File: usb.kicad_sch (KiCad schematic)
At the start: 0 parts

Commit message: merged in USB
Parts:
- added IC1: USB Hub, QFP80P900X900X160-32N, symbol group127:USB Hub
- added J1, J2: 2-Port USB, CONN_AU-Y1008-2_ASM, symbol group127:2-Port USB

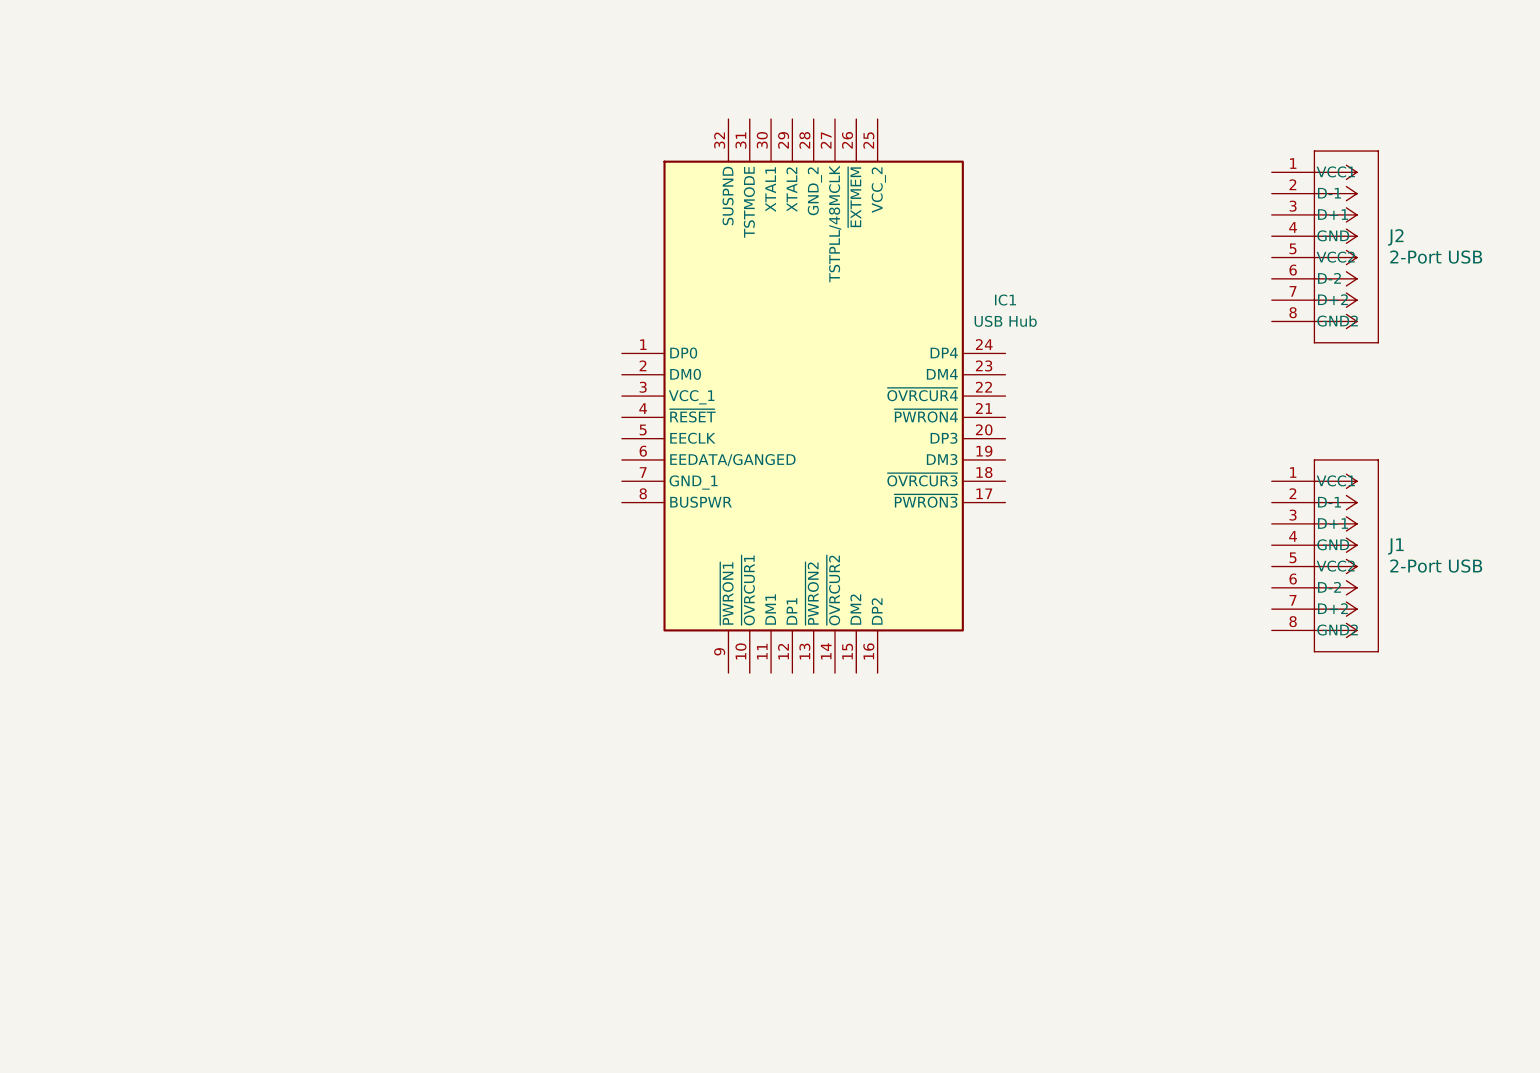
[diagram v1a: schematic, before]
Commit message: usb hub support completed
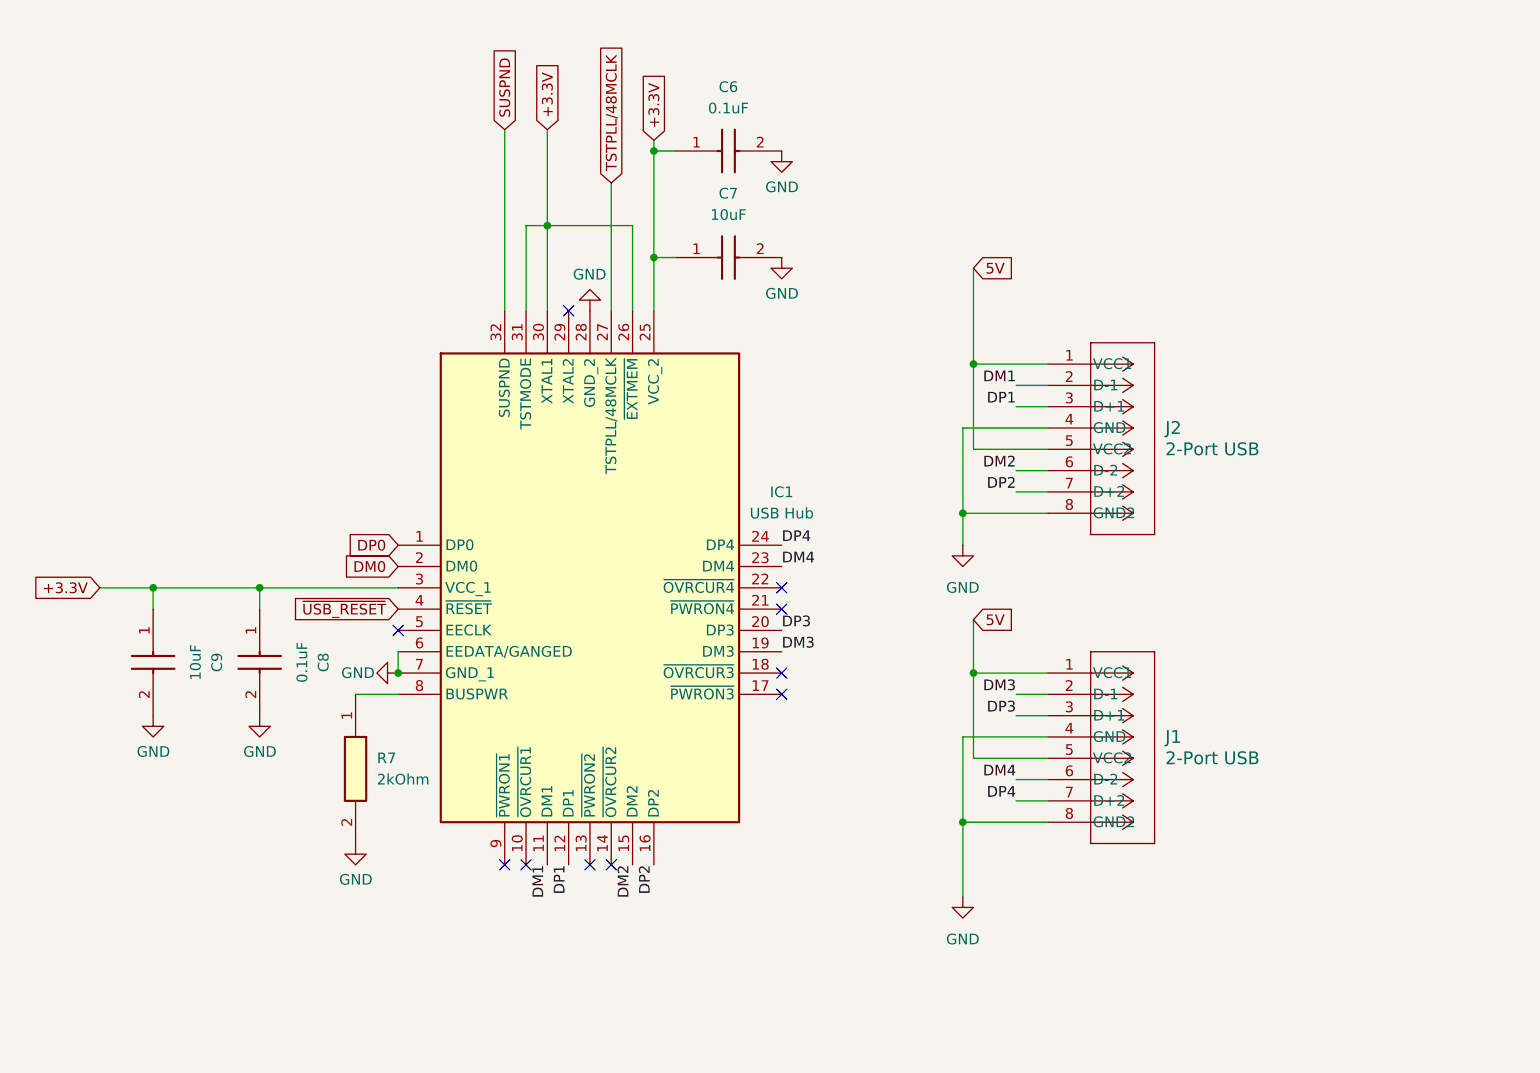
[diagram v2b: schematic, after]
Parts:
- added C6, C8: 0.1uF, CAPC2012X94N, symbol group127:0805Capacitor
- added C7, C9: 10uF, CAPC2012X94N, symbol group127:0805Capacitor
- added R7: 2kOhm, RESC2012X60N, symbol group127:Resistor
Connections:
- net 5V: now reaches J1.1 (VCC1)
- net 5V: now also J1.5 (VCC2), J2.1 (VCC1), J2.5 (VCC2)
- net DM3: now reaches J1.2 (D-1)
- net DM3: now also IC1.19 (DM3)
- net DP3: now reaches J1.3 (D+1)
- net DP3: now also IC1.20 (DP3)
- net GND: now reaches J1.4 (GND)
- net GND: now also IC1.28 (GND_2), IC1.6 (EEDATA/GANGED), IC1.7 (GND_1), J1.8 (GND2), J2.4 (GND), J2.8 (GND2), C6.2, C7.2, C8.2, C9.2, R7.2
- net DM4: now reaches J1.6 (D-2)
- net DM4: now also IC1.23 (DM4)
- net DP4: now reaches J1.7 (D+2)
- net DP4: now also IC1.24 (DP4)
- net DM1: now reaches J2.2 (D-1)
- net DM1: now also IC1.11 (DM1)
- net DP1: now reaches J2.3 (D+1)
- net DP1: now also IC1.12 (DP1)
- net DM2: now reaches J2.6 (D-2)
- net DM2: now also IC1.15 (DM2)
- net DP2: now reaches J2.7 (D+2)
- net DP2: now also IC1.16 (DP2)
- net DP0: now reaches IC1.1 (DP0)
- net DM0: now reaches IC1.2 (DM0)
- net +3.3V: now reaches IC1.25 (VCC_2)
- net +3.3V: now also IC1.26 (~{EXTMEM}), IC1.3 (VCC_1), IC1.30 (XTAL1), IC1.31 (TSTMODE), C6.1, C7.1, C8.1, C9.1
- net TSTPLL/48MCLK: now reaches IC1.27 (TSTPLL/48MCLK)
- net SUSPND: now reaches IC1.32 (SUSPND)
- net ~{USB_RESET}: now reaches IC1.4 (~{RESET})
- net at IC1.8 (BUSPWR): now also R7.1
- no-connect marks 0 -> 10
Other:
- moved on the sheet: IC1, J1, J2

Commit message: standardize 5V and 3V3 labels
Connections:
- net +3.3V renamed 3V3
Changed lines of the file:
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@@
 		)
 	)
-	(global_label "+3.3V"
+	(global_label "3V3"
+		(shape input)
+		(at 73.66 102.87 180)
+		(fields_autoplaced yes)
+		(effects
+			(font
+				(size 1.27 1.27)
+			)
+			(justify right)
+		)
+		(property "Intersheetrefs" "${INTERSHEET_REFS}"
+			(at 67.1672 102.87 0)
+			(effects
+				(font
+					(size 1.27 1.27)
+				)
+				(justify right)
+				(hide yes)
+			)
+		)
+	)
+	(global_label "3V3"
 		(shape input)
 		(at 139.7 49.53 90)
+		(fields_autoplaced yes)
 		(effects
 			(font
@@
 		)
 		(property "Intersheetrefs" "${INTERSHEET_REFS}"
-			(at 139.7 49.53 0)
+			(at 139.7 43.0372 90)
 			(effects
 				(font
 					(size 1.27 1.27)
 				)
+				(justify left)
 				(hide yes)
 			)
@@
 		)
 	)
-	(global_label "+3.3V"
-		(shape input)
-		(at 73.66 102.87 180)
-		(effects
-			(font
-				(size 1.27 1.27)
-			)
-			(justify right)
-		)
-		(property "Intersheetrefs" "${INTERSHEET_REFS}"
-			(at 73.66 102.87 0)
-			(effects
-				(font
-					(size 1.27 1.27)
-				)
-				(hide yes)
-			)
-		)
-	)
-	(global_label "+3.3V"
-		(shape input)
-		(at 127 48.26 90)
-		(effects
-			(font
-				(size 1.27 1.27)
-			)
-			(justify left)
-		)
-		(property "Intersheetrefs" "${INTERSHEET_REFS}"
-			(at 127 48.26 0)
-			(effects
-				(font
-					(size 1.27 1.27)
-				)
-				(hide yes)
-			)
-		)
-	)
 	(global_label "5V"
 		(shape input)
@@
 			(effects
 				(font
+					(size 1.27 1.27)
+				)
+				(justify left)
+				(hide yes)
+			)
+		)
+	)
+	(global_label "3V3"
+		(shape input)
+		(at 127 48.26 90)
+		(fields_autoplaced yes)
+		(effects
+			(font
+				(size 1.27 1.27)
+			)
+			(justify left)
+		)
+		(property "Intersheetrefs" "${INTERSHEET_REFS}"
+			(at 127 41.7672 90)
+			(effects
+				(font

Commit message: finished up schematic
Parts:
- C2: renamed from C9; footprint CAPC2012X94N -> Capacitor_SMD:C_0805_2012Metric
- C3: renamed from C8; footprint CAPC2012X94N -> Capacitor_SMD:C_0805_2012Metric
- C4: renamed from C6; footprint CAPC2012X94N -> Capacitor_SMD:C_0805_2012Metric
- C5: renamed from C7; footprint CAPC2012X94N -> Capacitor_SMD:C_0805_2012Metric
- IC2: renamed from IC1; footprint QFP80P900X900X160-32N -> (none)
- J2: footprint CONN_AU-Y1008-2_ASM -> (none)
- J3: renamed from J1; footprint CONN_AU-Y1008-2_ASM -> (none)
- R1: renamed from R7; footprint RESC2012X60N -> Resistor_SMD:R_0805_2012Metric
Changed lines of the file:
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@@
 		(dnp no)
 		(fields_autoplaced yes)
-		(property "Reference" "R7"
+		(property "Reference" "R1"
 			(at 106.68 123.1899 90)
 			(effects
@@
 			)
 		)
-		(property "Footprint" "RESC2012X60N"
+		(property "Footprint" "Resistor_SMD:R_0805_2012Metric"
 			(at 7.95 129.54 0)
 			(effects
@@
 			(project ""
 				(path "/5ce3566e-4e0f-420e-9b0d-3952cd3c63fd/5f7ff1a1-baeb-4db3-a7fc-b3c90c01be12"
-					(reference "R7")
+					(reference "R1")
 					(unit 1)
 				)
@@
 		(dnp no)
 		(fields_autoplaced yes)
-		(property "Reference" "C7"
+		(property "Reference" "C5"
 			(at 148.59 55.88 0)
 			(effects
@@
 			)
 		)
-		(property "Footprint" "CAPC2012X94N"
+		(property "Footprint" "Capacitor_SMD:C_0805_2012Metric"
 			(at 151.13 159.69 0)
 			(effects
@@
 			(project ""
 				(path "/5ce3566e-4e0f-420e-9b0d-3952cd3c63fd/5f7ff1a1-baeb-4db3-a7fc-b3c90c01be12"
-					(reference "C7")
+					(reference "C5")
 					(unit 1)
 				)
@@
 		(dnp no)
 		(fields_autoplaced yes)
-		(property "Reference" "J1"
+		(property "Reference" "J3"
 			(at 200.66 120.6499 0)
 			(effects
@@
 			)
 		)
-		(property "Footprint" "CONN_AU-Y1008-2_ASM"
+		(property "Footprint" ""
 			(at 179.324 135.382 0)
 			(effects
@@
 			(project ""
 				(path "/5ce3566e-4e0f-420e-9b0d-3952cd3c63fd/5f7ff1a1-baeb-4db3-a7fc-b3c90c01be12"
-					(reference "J1")
+					(reference "J3")
 					(unit 1)
 				)
@@
 		(on_board yes)
 		(dnp no)
-		(property "Reference" "#PWR015"
+		(property "Reference" "#PWR012"
 			(at 102.87 113.03 0)
 			(effects
@@
 			(project ""
 				(path "/5ce3566e-4e0f-420e-9b0d-3952cd3c63fd/5f7ff1a1-baeb-4db3-a7fc-b3c90c01be12"
-					(reference "#PWR015")
+					(reference "#PWR012")
 					(unit 1)
 				)
@@
 			)
 		)
-		(property "Footprint" "CONN_AU-Y1008-2_ASM"
+		(property "Footprint" ""
 			(at 179.324 98.552 0)
 			(effects
@@
 		(dnp no)
 		(fields_autoplaced yes)
-		(property "Reference" "C9"
+		(property "Reference" "C2"
 			(at 87.63 111.76 0)
 			(effects
@@
 			)
 		)
-		(property "Footprint" "CAPC2012X94N"
+		(property "Footprint" "Capacitor_SMD:C_0805_2012Metric"
 			(at -16.18 114.3 0)
 			(effects
@@
 			(project "harm_drone"
 				(path "/5ce3566e-4e0f-420e-9b0d-3952cd3c63fd/5f7ff1a1-baeb-4db3-a7fc-b3c90c01be12"
-					(reference "C9")
+					(reference "C2")
 					(unit 1)
 				)
@@
 		(on_board yes)
 		(dnp no)
-		(property "Reference" "#PWR019"
+		(property "Reference" "#PWR011"
 			(at 104.14 139.7 0)
 			(effects
@@
 			(project "harm_drone"
 				(path "/5ce3566e-4e0f-420e-9b0d-3952cd3c63fd/5f7ff1a1-baeb-4db3-a7fc-b3c90c01be12"
-					(reference "#PWR019")
+					(reference "#PWR011")
 					(unit 1)
 				)
@@
 		(dnp no)
 		(fields_autoplaced yes)
-		(property "Reference" "C8"
+		(property "Reference" "C3"
 			(at 100.33 111.76 0)
 			(effects
@@
 			)
 		)
-		(property "Footprint" "CAPC2012X94N"
+		(property "Footprint" "Capacitor_SMD:C_0805_2012Metric"
 			(at -3.48 114.3 0)
 			(effects
@@
 			(project "harm_drone"
 				(path "/5ce3566e-4e0f-420e-9b0d-3952cd3c63fd/5f7ff1a1-baeb-4db3-a7fc-b3c90c01be12"
-					(reference "C8")
+					(reference "C3")
 					(unit 1)
 				)
@@
 		(on_board yes)
 		(dnp no)
-		(property "Reference" "#PWR04"
+		(property "Reference" "#PWR015"
 			(at 154.94 69.85 0)
 			(effects
@@
 			(project "harm_drone"
 				(path "/5ce3566e-4e0f-420e-9b0d-3952cd3c63fd/5f7ff1a1-baeb-4db3-a7fc-b3c90c01be12"
-					(reference "#PWR04")
+					(reference "#PWR015")
 					(unit 1)
 				)
@@
 		(dnp no)
 		(fields_autoplaced yes)
-		(property "Reference" "#PWR02"
+		(property "Reference" "#PWR017"
 			(at 176.53 146.05 0)
 			(effects
@@
 			(project "harm_drone"
 				(path "/5ce3566e-4e0f-420e-9b0d-3952cd3c63fd/5f7ff1a1-baeb-4db3-a7fc-b3c90c01be12"
-					(reference "#PWR02")
+					(reference "#PWR017")
 					(unit 1)
 				)
@@
 		(on_board yes)
 		(dnp no)
-		(property "Reference" "#PWR018"
+		(property "Reference" "#PWR09"
 			(at 80.01 124.46 0)
 			(effects
@@
 			(project "harm_drone"
 				(path "/5ce3566e-4e0f-420e-9b0d-3952cd3c63fd/5f7ff1a1-baeb-4db3-a7fc-b3c90c01be12"
-					(reference "#PWR018")
+					(reference "#PWR09")
 					(unit 1)
 				)
@@
 		(dnp no)
 		(fields_autoplaced yes)
-		(property "Reference" "C6"
+		(property "Reference" "C4"
 			(at 148.59 43.18 0)
 			(effects
@@
 			)
 		)
-		(property "Footprint" "CAPC2012X94N"
+		(property "Footprint" "Capacitor_SMD:C_0805_2012Metric"
 			(at 151.13 146.99 0)
 			(effects
@@
 			(project ""
 				(path "/5ce3566e-4e0f-420e-9b0d-3952cd3c63fd/5f7ff1a1-baeb-4db3-a7fc-b3c90c01be12"
-					(reference "C6")
+					(reference "C4")
 					(unit 1)
 				)
@@
 		(dnp no)
 		(fields_autoplaced yes)
-		(property "Reference" "IC1"
+		(property "Reference" "IC2"
 			(at 154.94 91.4714 0)
 			(effects
@@
 			)
 		)
-		(property "Footprint" "QFP80P900X900X160-32N"
+		(property "Footprint" ""
 			(at 151.13 172.39 0)
 			(effects
@@
 			(project ""
 				(path "/5ce3566e-4e0f-420e-9b0d-3952cd3c63fd/5f7ff1a1-baeb-4db3-a7fc-b3c90c01be12"
-					(reference "IC1")
+					(reference "IC2")
 					(unit 1)
 				)
@@
 		(on_board yes)
 		(dnp no)
-		(property "Reference" "#PWR03"
+		(property "Reference" "#PWR014"
 			(at 154.94 57.15 0)
 			(effects
@@
 			(project "harm_drone"
 				(path "/5ce3566e-4e0f-420e-9b0d-3952cd3c63fd/5f7ff1a1-baeb-4db3-a7fc-b3c90c01be12"
-					(reference "#PWR03")
+					(reference "#PWR014")
 					(unit 1)
 				)
@@
 		(on_board yes)
 		(dnp no)
-		(property "Reference" "#PWR017"
+		(property "Reference" "#PWR010"
 			(at 92.71 124.46 0)
 			(effects
@@
 			(project "harm_drone"
 				(path "/5ce3566e-4e0f-420e-9b0d-3952cd3c63fd/5f7ff1a1-baeb-4db3-a7fc-b3c90c01be12"
-					(reference "#PWR017")
+					(reference "#PWR010")
 					(unit 1)
 				)
@@
 		(dnp no)
 		(fields_autoplaced yes)
-		(property "Reference" "#PWR01"
+		(property "Reference" "#PWR016"
 			(at 176.53 104.14 0)
 			(effects
@@
 			(project "harm_drone"
 				(path "/5ce3566e-4e0f-420e-9b0d-3952cd3c63fd/5f7ff1a1-baeb-4db3-a7fc-b3c90c01be12"
-					(reference "#PWR01")
+					(reference "#PWR016")
 					(unit 1)
 				)
@@
 		(on_board yes)
 		(dnp no)
-		(property "Reference" "#PWR016"
+		(property "Reference" "#PWR013"
 			(at 132.08 63.5 0)
 			(effects
@@
 			(project ""
 				(path "/5ce3566e-4e0f-420e-9b0d-3952cd3c63fd/5f7ff1a1-baeb-4db3-a7fc-b3c90c01be12"
-					(reference "#PWR016")
-					(unit 1)
-				)
+					(reference "#PWR013")
+					(unit 1)
+				)

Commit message: initial PCB draft!
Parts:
- IC2: footprint (none) -> group127:USB-HUB; symbol group127:USB Hub -> group127:USB-HUB
- J2, J3: footprint (none) -> group127:USBPorts
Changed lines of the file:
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@@
 			)
 		)
-		(property "Footprint" ""
+		(property "Footprint" "group127:USBPorts"
 			(at 179.324 135.382 0)
 			(effects
@@
 			)
 		)
-		(property "Footprint" ""
+		(property "Footprint" "group127:USBPorts"
 			(at 179.324 98.552 0)
 			(effects
@@
 	)
 	(symbol
-		(lib_id "group127:USB Hub")
+		(lib_id "group127:USB-HUB")
 		(at 109.22 97.79 0)
 		(unit 1)
@@
 			)
 		)
-		(property "Footprint" ""
+		(property "Footprint" "group127:USB-HUB"
 			(at 151.13 172.39 0)
 			(effects

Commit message: namespace change
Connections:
- net DM0 renamed D0-
- net DM1 renamed D1-
- net DM2 renamed D2-
- net DM3 renamed D3-
- net DM4 renamed D4-
- net DP0 renamed D0+
- net DP1 renamed D1+
- net DP2 renamed D2+
- net DP3 renamed D3+
- net DP4 renamed D4+
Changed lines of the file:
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@@
 		)
 	)
-	(label "DM3"
+	(label "D3-"
 		(at 154.94 110.49 0)
 		(fields_autoplaced yes)
@@
 		)
 	)
-	(label "DP4"
+	(label "D4+"
 		(at 154.94 97.79 0)
 		(fields_autoplaced yes)
@@
 		)
 	)
-	(label "DM1"
+	(label "D1-"
 		(at 182.88 78.74 180)
 		(fields_autoplaced yes)
@@
 		)
 	)
-	(label "DM4"
+	(label "D4-"
 		(at 154.94 100.33 0)
 		(fields_autoplaced yes)
@@
 		)
 	)
-	(label "DP3"
+	(label "D3+"
 		(at 182.88 118.11 180)
 		(fields_autoplaced yes)
@@
 		)
 	)
-	(label "DP2"
+	(label "D2+"
 		(at 182.88 91.44 180)
 		(fields_autoplaced yes)
@@
 		)
 	)
-	(label "DP3"
+	(label "D3+"
 		(at 154.94 107.95 0)
 		(fields_autoplaced yes)
@@
 		)
 	)
-	(label "DM1"
+	(label "D1-"
 		(at 127 135.89 270)
 		(fields_autoplaced yes)
@@
 		)
 	)
-	(label "DP2"
+	(label "D2+"
 		(at 139.7 135.89 270)
 		(fields_autoplaced yes)
@@
 		)
 	)
-	(label "DP1"
+	(label "D1+"
 		(at 182.88 81.28 180)
 		(fields_autoplaced yes)
@@
 		)
 	)
-	(label "DM2"
+	(label "D2-"
 		(at 182.88 88.9 180)
 		(fields_autoplaced yes)
@@
 		)
 	)
-	(label "DP1"
+	(label "D1+"
 		(at 129.54 135.89 270)
 		(fields_autoplaced yes)
@@
 		)
 	)
-	(label "DP4"
+	(label "D4+"
 		(at 182.88 128.27 180)
 		(fields_autoplaced yes)
@@
 		)
 	)
-	(label "DM3"
+	(label "D3-"
 		(at 182.88 115.57 180)
 		(fields_autoplaced yes)
@@
 		)
 	)
-	(label "DM2"
+	(label "D2-"
 		(at 137.16 135.89 270)
 		(fields_autoplaced yes)
@@
 		)
 	)
-	(label "DM4"
+	(label "D4-"
 		(at 182.88 125.73 180)
 		(fields_autoplaced yes)
@@
 		)
 	)
-	(global_label "DM0"
+	(global_label "D0-"
 		(shape input)
 		(at 109.22 100.33 180)
@@
 		)
 	)
-	(global_label "DP0"
+	(global_label "D0+"
 		(shape input)
 		(at 109.22 97.79 180)

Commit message: schematic fixes are done
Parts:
- added R16, R21, R22, R27, R28, R29, R30: 15kOhm, RESC2012X60N, symbol group127:Resistor
- added R17, R18, R19, R20, R23, R24, R25, R26: 27ohm, RESC2012X60N, symbol group127:Resistor
- R1: value 2kOhm -> 15kOhm; footprint Resistor_SMD:R_0805_2012Metric -> RESC2012X60N
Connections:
- net D1+: now also R18.1; no longer J2.3 (D+1)
- net D1-: now also R17.1; no longer J2.2 (D-1)
- net D2+: now also R20.1; no longer J2.7 (D+2)
- net D2-: now also R19.1; no longer J2.6 (D-2)
- net D3+: now also R24.1; no longer J3.3 (D+1)
- net D3-: now also R23.1; no longer J3.2 (D-1)
- net D4+: now also R26.1; no longer J3.7 (D+2)
- net D4-: now also R25.1; no longer J3.6 (D-2)
- net GND: now also IC2.8 (BUSPWR), R1.1, R16.1, R21.1, R22.1, R27.1, R28.1, R29.1, R30.1; no longer R1.2
- new net: J3.3 (D+1), R24.2, R28.2
- new net: J3.2 (D-1), R23.2, R27.2
- new net: J3.6 (D-2), R25.2, R29.2
- new net: J3.7 (D+2), R26.2, R30.2
- new net: J2.2 (D-1), R16.2, R17.2
- new net: J2.3 (D+1), R1.2, R18.2
- new net: J2.6 (D-2), R19.2, R21.2
- new net: J2.7 (D+2), R20.2, R22.2
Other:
- moved on the sheet: J2, J3

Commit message: final changes
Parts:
- R1: renamed from R17; footprint RESC2012X60N -> Resistor_SMD:R_0805_2012Metric
- R10: renamed from R27; footprint RESC2012X60N -> Resistor_SMD:R_0805_2012Metric
- R11: renamed from R1; footprint RESC2012X60N -> Resistor_SMD:R_0805_2012Metric
- R12: renamed from R28; footprint RESC2012X60N -> Resistor_SMD:R_0805_2012Metric
- R13: renamed from R21; footprint RESC2012X60N -> Resistor_SMD:R_0805_2012Metric
- R14: renamed from R29; footprint RESC2012X60N -> Resistor_SMD:R_0805_2012Metric
- R15: renamed from R22; footprint RESC2012X60N -> Resistor_SMD:R_0805_2012Metric
- R16: renamed from R30; footprint RESC2012X60N -> Resistor_SMD:R_0805_2012Metric
- R2: renamed from R18; footprint RESC2012X60N -> Resistor_SMD:R_0805_2012Metric
- R3: renamed from R19; footprint RESC2012X60N -> Resistor_SMD:R_0805_2012Metric
- R4: renamed from R20; footprint RESC2012X60N -> Resistor_SMD:R_0805_2012Metric
- R5: renamed from R23; footprint RESC2012X60N -> Resistor_SMD:R_0805_2012Metric
- R6: renamed from R24; footprint RESC2012X60N -> Resistor_SMD:R_0805_2012Metric
- R7: renamed from R25; footprint RESC2012X60N -> Resistor_SMD:R_0805_2012Metric
- R8: renamed from R26; footprint RESC2012X60N -> Resistor_SMD:R_0805_2012Metric
- R9: renamed from R16; footprint RESC2012X60N -> Resistor_SMD:R_0805_2012Metric
- renumbered C2 to C14, C3 to C15, C4 to C16, C5 to C17
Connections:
- net J3_D1+: now reaches J3.3 (D+1), R12.2, R6.2
- net J3_D1-: now reaches J3.2 (D-1), R10.2, R5.2
- net J3_D2-: now reaches J3.6 (D-2), R14.2, R7.2
- net J3_D2+: now reaches J3.7 (D+2), R16.2, R8.2
- net J2_D1-: now reaches J2.2 (D-1), R1.2, R9.2
- net J2_D1+: now reaches J2.3 (D+1), R11.2, R2.2
- net J2_D2-: now reaches J2.6 (D-2), R13.2, R3.2
- net J2_D2+: now reaches J2.7 (D+2), R15.2, R4.2
